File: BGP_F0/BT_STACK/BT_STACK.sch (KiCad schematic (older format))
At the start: 18 parts, among them P1 CONN_01X05, P2 CONN_01X02, P3 CONN_01X04, U1 MC33178

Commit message: Removed old boards, all F0 are now 26mm deep
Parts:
- RV1: footprint LIBS:Potentiometer_Alps_RK097_Double_Vertical_Dual_Shaft -> LIBS:Potentiometer_Alpha_Double_Vertical_Dual_Shaft
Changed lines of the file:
@@
 F 0 "RV1" H 5460 5510 50  0000 C CNN
 F 1 "DUAL_POT" H 5590 4900 50  0000 C CNN
-F 2 "LIBS:Potentiometer_Alps_RK097_Double_Vertical_Dual_Shaft" H 5300 5200 50  0001 C CNN
+F 2 "LIBS:Potentiometer_Alpha_Double_Vertical_Dual_Shaft" H 5300 5200 50  0001 C CNN
 F 3 "" H 5300 5200 50  0000 C CNN
 	1    5300 5200
@@
 $EndComp
 $Comp
-L Earth #PWR1
+L Earth #PWR01
 U 1 1 5A5AEE2D
 P 3950 2700
-F 0 "#PWR1" H 3950 2450 50  0001 C CNN
+F 0 "#PWR01" H 3950 2450 50  0001 C CNN
 F 1 "Earth" H 3950 2550 50  0001 C CNN
 F 2 "" H 3950 2700 50  0001 C CNN
@@
 Vref
 $Comp
-L Earth #PWR2
+L Earth #PWR02
 U 1 1 5A66674C
 P 4400 2600
-F 0 "#PWR2" H 4400 2350 50  0001 C CNN
+F 0 "#PWR02" H 4400 2350 50  0001 C CNN
 F 1 "Earth" H 4400 2450 50  0001 C CNN
 F 2 "" H 4400 2600 50  0001 C CNN
@@
 $EndComp
 $Comp
-L Earth #PWR3
+L Earth #PWR03
 U 1 1 5A666795
 P 5300 3000
-F 0 "#PWR3" H 5300 2750 50  0001 C CNN
+F 0 "#PWR03" H 5300 2750 50  0001 C CNN
 F 1 "Earth" H 5300 2850 50  0001 C CNN
 F 2 "" H 5300 3000 50  0001 C CNN
@@
 V+
 $Comp
-L Earth #PWR4
+L Earth #PWR04
 U 1 1 5A666848
 P 7100 3000
-F 0 "#PWR4" H 7100 2750 50  0001 C CNN
+F 0 "#PWR04" H 7100 2750 50  0001 C CNN
 F 1 "Earth" H 7100 2850 50  0001 C CNN
 F 2 "" H 7100 3000 50  0001 C CNN

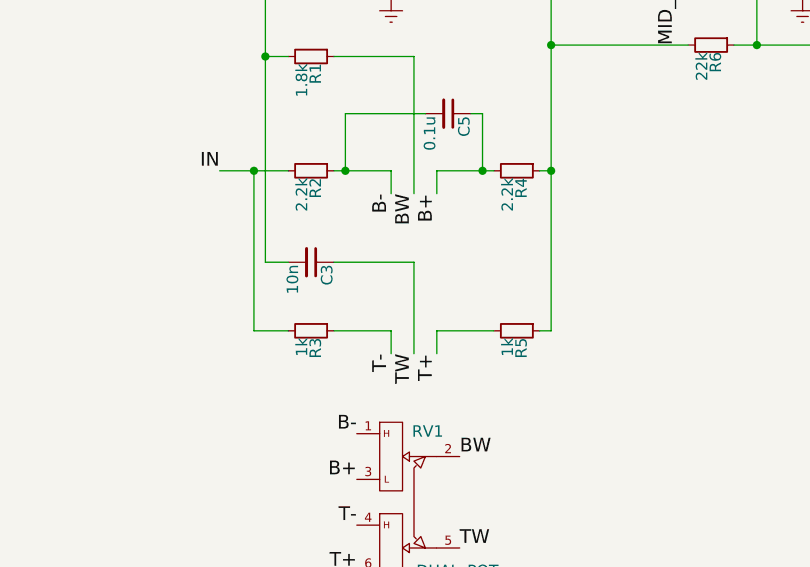
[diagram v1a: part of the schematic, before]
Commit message: BT and MID pot gain ctrl reversed for proper action
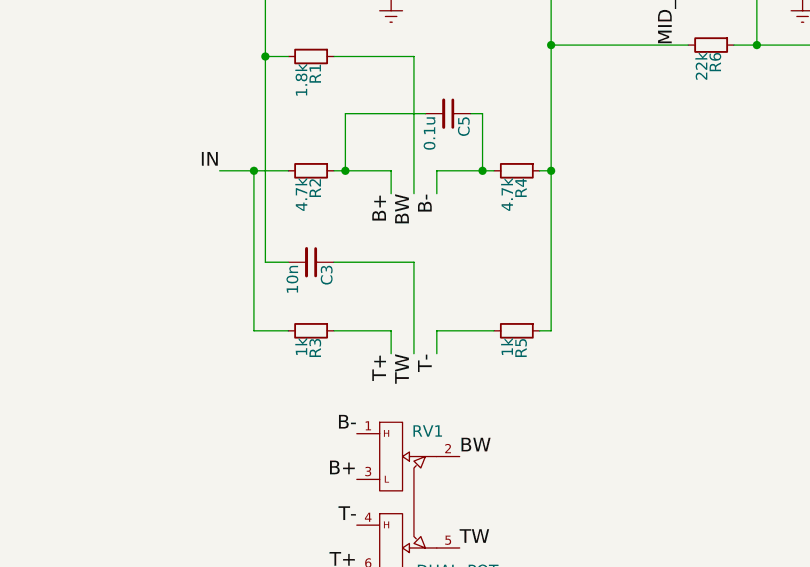
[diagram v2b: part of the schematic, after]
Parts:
- R2, R4: value 2.2k -> 4.7k
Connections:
- net B+: now also C5.2, R2.1; no longer C5.1, R4.2
- net B-: now also C5.1, R4.2; no longer C5.2, R2.1
- net T+: now also R3.1; no longer R5.2
- net T-: now also R5.2; no longer R3.1
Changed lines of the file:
@@
 P 4950 3750
 F 0 "R2" H 4980 3770 50  0000 L CNN
-F 1 "2.2k" H 4980 3710 50  0000 L CNN
+F 1 "4.7k" H 4980 3710 50  0000 L CNN
 F 2 "Resistors_SMD:R_0603_HandSoldering" H 4950 3750 50  0001 C CNN
 F 3 "" H 4950 3750 50  0000 C CNN
@@
 P 5850 3750
 F 0 "R4" H 5880 3770 50  0000 L CNN
-F 1 "2.2k" H 5880 3710 50  0000 L CNN
+F 1 "4.7k" H 5880 3710 50  0000 L CNN
 F 2 "Resistors_SMD:R_0603_HandSoldering" H 5850 3750 50  0001 C CNN
 F 3 "" H 5850 3750 50  0000 C CNN
@@
 	0    1    1    0
 $EndComp
+Text Label 5500 3850 3    60   ~ 0
+B-
 Text Label 5300 3850 3    60   ~ 0
-B-
-Text Label 5500 3850 3    60   ~ 0
 B+
 Text Label 5400 3850 3    60   ~ 0
@@
 	4700 4450 4700 3750
 Connection ~ 4700 3750
+Text Label 5500 4550 3    60   ~ 0
+T-
 Text Label 5300 4550 3    60   ~ 0
-T-
-Text Label 5500 4550 3    60   ~ 0
 T+
 Text Label 5400 4550 3    60   ~ 0

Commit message: F0 Final
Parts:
- C4: footprint Capacitors_SMD:C_0805_HandSoldering -> Capacitors_SMD:C_0603
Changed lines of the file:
@@
 F 0 "C4" H 5310 2170 50  0000 L CNN
 F 1 "470p" H 5310 2020 50  0000 L CNN
-F 2 "Capacitors_SMD:C_0805_HandSoldering" H 5300 2100 50  0001 C CNN
+F 2 "Capacitors_SMD:C_0603" H 5300 2100 50  0001 C CNN
 F 3 "" H 5300 2100 50  0000 C CNN
 	1    5300 2100

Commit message: Various - BOM complete
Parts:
- added C6: 470p, Capacitors_SMD:C_0603, symbol C_Small
- R2, R4: value 4.7k -> 4.99k
- R6, R7: value 22k -> 20k
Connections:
- net at R6.1, R7.2, U1.6 (-): now also C6.2
- net at R7.1, R8.2, U1.7: now also C6.1
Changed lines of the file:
@@
 P 4950 3750
 F 0 "R2" H 4980 3770 50  0000 L CNN
-F 1 "4.7k" H 4980 3710 50  0000 L CNN
+F 1 "4.99k" H 4980 3710 50  0000 L CNN
 F 2 "Resistors_SMD:R_0603_HandSoldering" H 4950 3750 50  0001 C CNN
 F 3 "" H 4950 3750 50  0000 C CNN
@@
 P 5850 3750
 F 0 "R4" H 5880 3770 50  0000 L CNN
-F 1 "4.7k" H 5880 3710 50  0000 L CNN
+F 1 "4.99k" H 5880 3710 50  0000 L CNN
 F 2 "Resistors_SMD:R_0603_HandSoldering" H 5850 3750 50  0001 C CNN
 F 3 "" H 5850 3750 50  0000 C CNN
@@
 P 6700 3200
 F 0 "R6" H 6730 3220 50  0000 L CNN
-F 1 "22k" H 6730 3160 50  0000 L CNN
+F 1 "20k" H 6730 3160 50  0000 L CNN
 F 2 "Resistors_SMD:R_0603_HandSoldering" H 6700 3200 50  0001 C CNN
 F 3 "" H 6700 3200 50  0000 C CNN
@@
 P 7400 3200
 F 0 "R7" H 7430 3220 50  0000 L CNN
-F 1 "22k" H 7430 3160 50  0000 L CNN
+F 1 "20k" H 7430 3160 50  0000 L CNN
 F 2 "Resistors_SMD:R_0603_HandSoldering" H 7400 3200 50  0001 C CNN
 F 3 "" H 7400 3200 50  0000 C CNN
@@
 	7550 2700 7500 2700
 Wire Wire Line
-	7500 2700 7500 3200
+	7500 2700 7500 3450
 Wire Wire Line
 	7300 3200 6800 3200
 Wire Wire Line
-	6900 3200 6900 2800
+	6900 2800 6900 3450
 Connection ~ 6900 3200
 Wire Wire Line
@@
 Text Label 8600 2400 2    60   ~ 0
 MID_O
+$Comp
+L C_Small C6
+U 1 1 5A7E145F
+P 7400 3450
+F 0 "C6" H 7410 3520 50  0000 L CNN
+F 1 "470p" H 7410 3370 50  0000 L CNN
+F 2 "Capacitors_SMD:C_0603" H 7400 3450 50  0001 C CNN
+F 3 "" H 7400 3450 50  0000 C CNN
+	1    7400 3450
+	0    1    1    0
+$EndComp
+Connection ~ 7500 3200
+Wire Wire Line
+	6900 3450 7300 3450
 $EndSCHEMATC

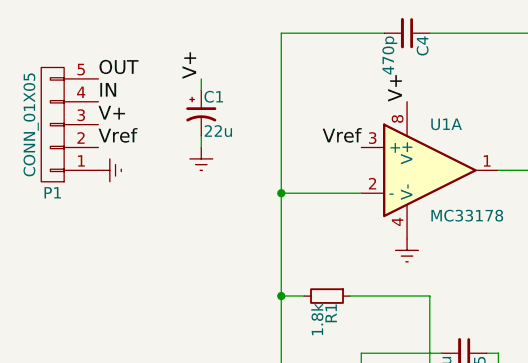
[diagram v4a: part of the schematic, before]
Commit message: Tone cap changed to female pin strip header for 0.047uF and 0.1uF
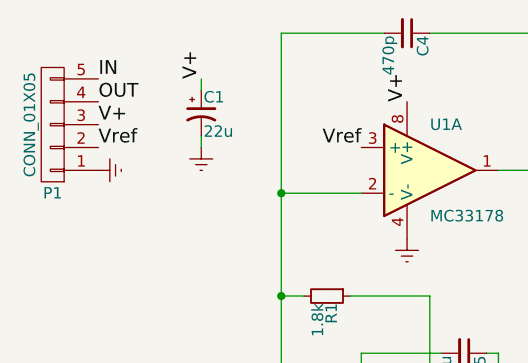
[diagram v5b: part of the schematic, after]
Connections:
- net IN: now also P1.5 (P5); no longer P1.4 (P4)
- net OUT: now also P1.4 (P4); no longer P1.5 (P5)
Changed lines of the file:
@@
 Text Label 3950 2500 0    60   ~ 0
 V+
+Text Label 3950 2400 0    60   ~ 0
+OUT
 Text Label 3950 2300 0    60   ~ 0
-OUT
-Text Label 3950 2400 0    60   ~ 0
 IN
 $Comp

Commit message: Mid Buff
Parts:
- removed P2: CONN_01X02, Pin_Headers:Pin_Header_Straight_1x02, symbol CONN_01X02
- added R9: 1.5MEG, Resistors_SMD:R_0603_HandSoldering, symbol R_Small
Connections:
- net MID_R: now also R9.1
- net Vref: now also R9.2
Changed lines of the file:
@@
 $EndComp
 $Comp
-L Earth #PWR01
+L Earth #PWR1
 U 1 1 5A5AEE2D
 P 3950 2700
-F 0 "#PWR01" H 3950 2450 50  0001 C CNN
+F 0 "#PWR1" H 3950 2450 50  0001 C CNN
 F 1 "Earth" H 3950 2550 50  0001 C CNN
 F 2 "" H 3950 2700 50  0001 C CNN
@@
 Vref
 $Comp
-L Earth #PWR02
+L Earth #PWR2
 U 1 1 5A66674C
 P 4400 2600
-F 0 "#PWR02" H 4400 2350 50  0001 C CNN
+F 0 "#PWR2" H 4400 2350 50  0001 C CNN
 F 1 "Earth" H 4400 2450 50  0001 C CNN
 F 2 "" H 4400 2600 50  0001 C CNN
@@
 $EndComp
 $Comp
-L Earth #PWR03
+L Earth #PWR3
 U 1 1 5A666795
 P 5300 3000
-F 0 "#PWR03" H 5300 2750 50  0001 C CNN
+F 0 "#PWR3" H 5300 2750 50  0001 C CNN
 F 1 "Earth" H 5300 2850 50  0001 C CNN
 F 2 "" H 5300 3000 50  0001 C CNN
@@
 V+
 $Comp
-L Earth #PWR04
+L Earth #PWR4
 U 1 1 5A666848
 P 7100 3000
-F 0 "#PWR04" H 7100 2750 50  0001 C CNN
+F 0 "#PWR4" H 7100 2750 50  0001 C CNN
 F 1 "Earth" H 7100 2850 50  0001 C CNN
 F 2 "" H 7100 3000 50  0001 C CNN
@@
 	7500 2700 7500 3450
 Wire Wire Line
-	7300 3200 6800 3200
+	6800 3200 7300 3200
 Wire Wire Line
 	6900 2800 6900 3450
@@
 	6600 3200 6000 3200
 Connection ~ 6000 3200
-$Comp
-L CONN_01X02 P2
-U 1 1 5A666CF7
-P 6700 2450
-F 0 "P2" H 6700 2600 50  0000 C CNN
-F 1 "CONN_01X02" V 6800 2450 50  0000 C CNN
-F 2 "Pin_Headers:Pin_Header_Straight_1x02" H 6700 2450 50  0001 C CNN
-F 3 "" H 6700 2450 50  0000 C CNN
-	1    6700 2450
-	-1   0    0    1
-$EndComp
 Wire Wire Line
 	6900 2600 6900 2500
-Wire Wire Line
-	6900 2400 6900 2300
-Text Label 6900 2300 1    60   ~ 0
+Text Label 6900 2250 1    60   ~ 0
 Vref
 Text Label 6550 3200 1    60   ~ 0
@@
 Wire Wire Line
 	6900 3450 7300 3450
+$Comp
+L R_Small R9
+U 1 1 5A88933C
+P 6900 2400
+F 0 "R9" H 6930 2420 50  0000 L CNN
+F 1 "1.5MEG" H 6930 2360 50  0000 L CNN
+F 2 "Resistors_SMD:R_0603_HandSoldering" H 6900 2400 50  0001 C CNN
+F 3 "" H 6900 2400 50  0000 C CNN
+	1    6900 2400
+	-1   0    0    1
+$EndComp
+Wire Wire Line
+	6900 2250 6900 2300
 $EndSCHEMATC

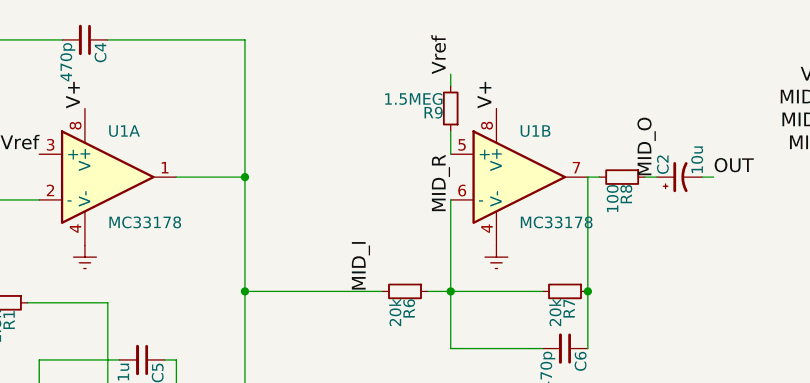
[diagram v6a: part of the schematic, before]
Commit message: Change some caps to TH, updated BOM - need to recreate
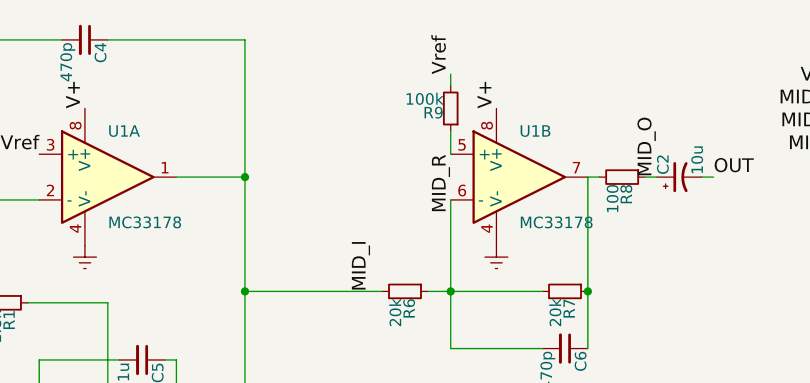
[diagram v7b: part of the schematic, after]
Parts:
- R9: value 1.5MEG -> 100k
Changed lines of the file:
@@
 P 6900 2400
 F 0 "R9" H 6930 2420 50  0000 L CNN
-F 1 "1.5MEG" H 6930 2360 50  0000 L CNN
+F 1 "100k" H 6930 2360 50  0000 L CNN
 F 2 "Resistors_SMD:R_0603_HandSoldering" H 6900 2400 50  0001 C CNN
 F 3 "" H 6900 2400 50  0000 C CNN

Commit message: Some extras
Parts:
- C4, C6: value 470p -> 270p
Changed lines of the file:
@@
 P 5300 2100
 F 0 "C4" H 5310 2170 50  0000 L CNN
-F 1 "470p" H 5310 2020 50  0000 L CNN
+F 1 "270p" H 5310 2020 50  0000 L CNN
 F 2 "Capacitors_SMD:C_0603" H 5300 2100 50  0001 C CNN
 F 3 "" H 5300 2100 50  0000 C CNN
@@
 $EndComp
 $Comp
-L Earth #PWR1
+L Earth #PWR01
 U 1 1 5A5AEE2D
 P 3950 2700
-F 0 "#PWR1" H 3950 2450 50  0001 C CNN
+F 0 "#PWR01" H 3950 2450 50  0001 C CNN
 F 1 "Earth" H 3950 2550 50  0001 C CNN
 F 2 "" H 3950 2700 50  0001 C CNN
@@
 Vref
 $Comp
-L Earth #PWR2
+L Earth #PWR02
 U 1 1 5A66674C
 P 4400 2600
-F 0 "#PWR2" H 4400 2350 50  0001 C CNN
+F 0 "#PWR02" H 4400 2350 50  0001 C CNN
 F 1 "Earth" H 4400 2450 50  0001 C CNN
 F 2 "" H 4400 2600 50  0001 C CNN
@@
 $EndComp
 $Comp
-L Earth #PWR3
+L Earth #PWR03
 U 1 1 5A666795
 P 5300 3000
-F 0 "#PWR3" H 5300 2750 50  0001 C CNN
+F 0 "#PWR03" H 5300 2750 50  0001 C CNN
 F 1 "Earth" H 5300 2850 50  0001 C CNN
 F 2 "" H 5300 3000 50  0001 C CNN
@@
 V+
 $Comp
-L Earth #PWR4
+L Earth #PWR04
 U 1 1 5A666848
 P 7100 3000
-F 0 "#PWR4" H 7100 2750 50  0001 C CNN
+F 0 "#PWR04" H 7100 2750 50  0001 C CNN
 F 1 "Earth" H 7100 2850 50  0001 C CNN
 F 2 "" H 7100 3000 50  0001 C CNN
@@
 P 7400 3450
 F 0 "C6" H 7410 3520 50  0000 L CNN
-F 1 "470p" H 7410 3370 50  0000 L CNN
+F 1 "270p" H 7410 3370 50  0000 L CNN
 F 2 "Capacitors_SMD:C_0603" H 7400 3450 50  0001 C CNN
 F 3 "" H 7400 3450 50  0000 C CNN
